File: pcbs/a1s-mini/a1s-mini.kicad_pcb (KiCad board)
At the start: 2 copper layers, 76 x 56 mm, 9 parts, among them IC1 3678, J5 Audio Out, U1 ESP32-DevKitC header, U2 CP2104 USB A board

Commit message: Starting A1S Mini, teardrops on sandwhich
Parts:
- removed IC1: 3678, DIY:Adafruit 3678
- removed JP1: SolderJumper_3_Bridged12, Jumper:SolderJumper-3_P1.3mm_Bridged12_RoundedPad1.0x1.5mm
- added 3V1: TestPoint_Small, TestPoint:TestPoint_Pad_D1.0mm, F.Cu at (108.4, 22.1)
- added 5V1: TestPoint_Small, TestPoint:TestPoint_Pad_D1.0mm, F.Cu at (109.5, 25.8)
- added C1: 0.1uF 50V, Capacitor_SMD:C_0805_2012Metric, F.Cu at (124.6, 60.8)
- added C10: 10uF, Capacitor_SMD:C_0805_2012Metric, F.Cu at (261.7, 126.9)
- added C11: 0.1uF 50V, Capacitor_SMD:C_0805_2012Metric, F.Cu at (261.7, 129.9)
- added C12: 10uF, Capacitor_SMD:C_0805_2012Metric, F.Cu at (257.5, 143.9)
- added C13: 10uF, Capacitor_SMD:C_0805_2012Metric, F.Cu at (127.3, 162.1)
- added C14: 0.1uF 50V, Capacitor_SMD:C_0805_2012Metric, F.Cu at (130.3, 162.1)
- added C15: 10uF, Capacitor_SMD:C_0805_2012Metric, F.Cu at (133.3, 162.1)
- added C2: 22uF, Capacitor_SMD:C_0805_2012Metric, F.Cu at (122.3, 60.8)
- added C3: 0.1uF 50V, Capacitor_SMD:C_0805_2012Metric, F.Cu at (152.0, 64.6)
- added C4: 0.1uF 50V, Capacitor_SMD:C_0805_2012Metric, F.Cu at (88.9, 121.0)
- added C5: 0.1uF 50V, Capacitor_SMD:C_0805_2012Metric, F.Cu at (65.8, 138.4)
- added C6: 22uF, Capacitor_SMD:C_0805_2012Metric, F.Cu at (138.7, 119.1)
- added C7: 22uF, Capacitor_SMD:C_0805_2012Metric, F.Cu at (135.6, 110.5)
- added C8: 0.1uF 50V, Capacitor_SMD:C_0805_2012Metric, F.Cu at (72.0, 97.9)
- added C9: 0.1uF 50V, Capacitor_SMD:C_0805_2012Metric, F.Cu at (78.1, 75.3)
- added D1: 2.1V G 10mA, LED_SMD:LED_0603_1608Metric, F.Cu at (135.2, 136.7)
- added D10: 1N5819HW-7-F, SamacSys_Parts:SOD3716X145N, F.Cu at (262.3, 147.1)
- added D11: LESD5D5.0CT1G, SamacSys_Parts:LESD5D50CT1G, F.Cu at (127.3, 166.2)
- added D12: LESD5D5.0CT1G, SamacSys_Parts:LESD5D50CT1G, F.Cu at (130.2, 166.2)
- added D13: LESD5D5.0CT1G, SamacSys_Parts:LESD5D50CT1G, F.Cu at (133.1, 166.2)
- added D14: 1N5819HW-7-F, SamacSys_Parts:SOD3716X145N, F.Cu at (137.9, 169.3)
- added D2: 2.1V G 10mA, LED_SMD:LED_0603_1608Metric, F.Cu at (135.2, 139.3)
- added D3: 2.1V G 10mA, LED_SMD:LED_0603_1608Metric, F.Cu at (250.4, 137.5)
- added D4: 2.1V G 10mA, LED_SMD:LED_0603_1608Metric, F.Cu at (250.4, 140.0)
- added D5: 2.1V O 10mA, LED_SMD:LED_0603_1608Metric, F.Cu at (131.8, 108.5)
- added D6: 2V R 10mA, LED_SMD:LED_0603_1608Metric, F.Cu at (154.6, 75.7)
- added D7: LESD5D5.0CT1G, SamacSys_Parts:LESD5D50CT1G, F.Cu at (254.2, 147.7)
- added D8: LESD5D5.0CT1G, SamacSys_Parts:LESD5D50CT1G, F.Cu at (252.1, 147.7)
- added D9: LESD5D5.0CT1G, SamacSys_Parts:LESD5D50CT1G, F.Cu at (258.5, 147.7)
- added DCD1: TestPoint_Small, TestPoint:TestPoint_Pad_D1.0mm, F.Cu at (110.2, 29.6)
- added GND1: TestPoint_Small, TestPoint:TestPoint_Pad_D1.0mm, F.Cu at (111.5, 33.8)
- added J1: UART1, Connector_PinHeader_2.54mm:PinHeader_1x04_P2.54mm_Vertical, F.Cu at (123.5, 162.2)
- added J2: SJ-3524-SMT-TR-PI, SamacSys_Parts:SJ3524SMTTRPI, F.Cu at (76.8, 135.0)
- added J3: Audio Out, Connector_PinHeader_2.54mm:PinHeader_1x03_P2.54mm_Vertical, F.Cu at (76.8, 110.8)
- added J4: UART0, Connector_PinHeader_2.54mm:PinHeader_1x04_P2.54mm_Vertical, F.Cu at (244.5, 119.8)
- added J6: USB4105-GF-A, DIY:GCT_USB4105-GF-A, F.Cu at (126.8, 156.5)
- added Q1: BC818, Package_TO_SOT_SMD:SOT-23, F.Cu at (68.8, 76.3)
- added Q2: BC818, Package_TO_SOT_SMD:SOT-23, F.Cu at (73.4, 76.0)
- added Q3: BC818, Package_TO_SOT_SMD:SOT-23, F.Cu at (228.2, 37.7)
- added Q4: BC818, Package_TO_SOT_SMD:SOT-23, F.Cu at (228.2, 42.2)
- added Q5: BC818, Package_TO_SOT_SMD:SOT-23, F.Cu at (228.2, 46.6)
- added R1: 1K 1%, Resistor_SMD:R_0805_2012Metric, F.Cu at (130.9, 136.9)
- added R10: 0R, Resistor_SMD:R_0805_2012Metric, F.Cu at (88.9, 126.9)
- added R11: 0R, Resistor_SMD:R_0805_2012Metric, F.Cu at (65.8, 144.3)
- added R12: 10K, Resistor_SMD:R_0805_2012Metric, F.Cu at (232.9, 37.0)
- added R13: 10K, Resistor_SMD:R_0805_2012Metric, F.Cu at (232.9, 39.9)
- added R14: 10K, Resistor_SMD:R_0805_2012Metric, F.Cu at (232.9, 42.9)
- added R15: 22.1K, Resistor_SMD:R_0805_2012Metric, F.Cu at (257.3, 119.6)
- added R16: 47.5K, Resistor_SMD:R_0805_2012Metric, F.Cu at (257.3, 122.6)
- added R17: 2K, Resistor_SMD:R_0805_2012Metric, F.Cu at (257.3, 125.5)
- added R18: 0R, Resistor_SMD:R_0805_2012Metric, F.Cu at (257.3, 128.5)
- added R19: 0R, Resistor_SMD:R_0805_2012Metric, F.Cu at (257.3, 131.4)
- added R2: 1K 1%, Resistor_SMD:R_0805_2012Metric, F.Cu at (130.9, 139.8)
- added R20: 5.1K 1%, Resistor_SMD:R_0805_2012Metric, F.Cu at (249.9, 147.7)
- added R21: 0R, Resistor_SMD:R_0805_2012Metric, F.Cu at (263.0, 152.7)
- added R22: 5.1K 1%, Resistor_SMD:R_0805_2012Metric, F.Cu at (256.4, 147.7)
- added R23: 22.1K, Resistor_SMD:R_0805_2012Metric, F.Cu at (122.6, 147.6)
- added R24: 47.5K, Resistor_SMD:R_0805_2012Metric, F.Cu at (125.6, 147.6)
- added R25: 2K, Resistor_SMD:R_0805_2012Metric, F.Cu at (128.5, 147.6)
- added R26: 0R, Resistor_SMD:R_0805_2012Metric, F.Cu at (131.5, 147.6)
- added R27: 0R, Resistor_SMD:R_0805_2012Metric, F.Cu at (134.4, 147.6)
- added R28: 5.1K 1%, Resistor_SMD:R_0805_2012Metric, F.Cu at (137.4, 147.6)
- added R29: 0R, Resistor_SMD:R_0805_2012Metric, F.Cu at (140.3, 147.6)
- added R3: 1K 1%, Resistor_SMD:R_0805_2012Metric, F.Cu at (246.1, 137.6)
- added R30: 5.1K 1%, Resistor_SMD:R_0805_2012Metric, F.Cu at (143.3, 147.6)
- added R4: 1K 1%, Resistor_SMD:R_0805_2012Metric, F.Cu at (246.1, 140.6)
- added R5: 1K 1%, Resistor_SMD:R_0805_2012Metric, F.Cu at (131.8, 110.5)
- added R6: 1K 1%, Resistor_SMD:R_0805_2012Metric, F.Cu at (154.7, 72.9)
- added R7: 0R, Resistor_SMD:R_0805_2012Metric, F.Cu at (148.0, 64.6)
- added R8: 22R 1%, Resistor_SMD:R_0805_2012Metric, F.Cu at (88.9, 124.0)
- added R9: 22R 1%, Resistor_SMD:R_0805_2012Metric, F.Cu at (65.8, 141.4)
- added S1: TL3305BF260QG, SamacSys_Parts:TL3305BF260QG, F.Cu at (74.2, 70.0)
- added S2: TL3305BF260QG, SamacSys_Parts:TL3305BF260QG, F.Cu at (77.5, 92.6)
- added U3: CP2102N, Package_DFN_QFN:QFN-28-1EP_5x5mm_P0.5mm_EP3.35x3.35mm, F.Cu at (263.1, 121.8)
- added U4: CP2102N, Package_DFN_QFN:QFN-28-1EP_5x5mm_P0.5mm_EP3.35x3.35mm, F.Cu at (138.5, 163.5)
- added VBUS1: TestPoint_Small, TestPoint:TestPoint_Pad_D1.0mm, F.Cu at (110.9, 37.2)
- J5: value Audio Out -> USB4105-GF-A; footprint Connector_PinHeader_2.54mm:PinHeader_1x03_P2.54mm_Vertical -> DIY:GCT_USB4105-GF-A
- U1: value ESP32-DevKitC header -> ESP32 A1S; footprint Espressif:ESP32-DevKitC -> Espressif:ESP32-WROVER-E_ThermalVias
- U2: value CP2104 USB A board -> AZ1117CH-3.3TRG1; footprint DIY:CP2104_USB_Board -> Package_TO_SOT_SMD:SOT-223-3_TabPin2; moved to F.Cu
- moved J5 150.2 mm to (254.1, 155.7), turned to 0 degrees
- moved H3 80.9 mm to (164.8, 35.0)
- moved H4 64.5 mm to (176.5, 36.9)
- moved H2 60.7 mm to (172.9, 29.0)
- moved U2 41.8 mm to (133.6, 116.3), turned to 90 degrees
- moved H1 39.0 mm to (155.6, 28.3)
- moved U1 32.0 mm to (135.9, 68.3)
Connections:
- U1 pad 1: +3.3V -> GND
- U1 pad 10: DIN -> unconnected-(U1-IO15-Pad10)
- U1 pad 11: BCLK -> IO2
- U1 pad 14: GND -> unconnected-(U1-MIC2N-Pad14)
- U1 pad 19: +5V -> GND
- U1 pad 2: unconnected-(U1-CHIP_PU-Pad2) -> +3.3V
- U1 pad 20: CLK -> GND
- U1 pad 21: D0 -> unconnected-(U1-LINEINR-Pad21)
- U1 pad 22: D1 -> unconnected-(U1-LINEINL-Pad22)
- U1 pad 23: GPIO15 -> unconnected-(U1-SPORP-Pad23)
- U1 pad 24: GPIO2 -> unconnected-(U1-SPORN-Pad24)
- U1 pad 25: GPIO0 -> unconnected-(U1-SPOLP-Pad25)
- U1 pad 26: GPIO4 -> unconnected-(U1-SPOLN-Pad26)
- U1 pad 27: GPIO16/U1RXD -> HPOUTL
- U1 pad 28: GPIO17/U1TXD -> HPOUTR
- U1 pad 29: GPIO5 -> unconnected-(U1-IO5-Pad29)
- U1 pad 30: GPIO18 -> IO18
- U1 pad 31: GPIO19 -> unconnected-(U1-IO23-Pad31)
- U1 pad 32: GND -> RXD1
- U1 pad 33: GPIO21 -> TXD1
- U1 pad 34: GPIO3/U0RXD -> unconnected-(U1-IO21-Pad34)
- U1 pad 35: GPIO1/U0TXD -> EN
- U1 pad 36: GPIO22 -> TXD0
- U1 pad 37: GPIO23 -> RXD0
- U1 pad 6: unconnected-(U1-VDET_2/GPIO35/ADC1_CH7-Pad6) -> IO0
- U1 pad 9: GPIO25 -> unconnected-(U1-IO13-Pad9)
- U2 pad 1: RST -> GND
- U2 pad 2: IO3 -> +3.3V
- U2 pad 3: IO2 -> +5V
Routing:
- net +5V: track 85.4 -> 0.00 mm
- net +3.3V: track 70.6 -> 0.00 mm
- net BCLK: track 37.3 -> 0.00 mm
- net DIN: track 34.3 -> 0.00 mm
- net GPIO25: track 33.1 -> 0.00 mm
- net GPIO16/U1RXD: track 22.4 -> 0.00 mm, vias 1 -> 0
- net GPIO17/U1TXD: track 22.1 -> 0.00 mm
- net GPIO4: track 13.7 -> 0.00 mm
- net ROUT: track 9.68 -> 0.00 mm
- net LOUT: track 9.68 -> 0.00 mm
- net AGND: track 9.68 -> 0.00 mm
- net DCD: track 6.35 -> 0.00 mm
- net GPIO5: track 2.54 -> 0.00 mm
- net GPIO3/U0RXD: track 2.54 -> 0.00 mm
- net GPIO23: track 2.54 -> 0.00 mm
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- removed copper zone on B.Cu, net GND
- removed copper zone on F.Cu, net GND
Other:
- board outline removed
- board text removed: "${TITLE} rev${REVISION} - (c) Martin Roger - ${ISSUE_DATE}"
- board text removed: "ANTENNA"
- board text removed: "G"
- board text removed: "GND"
- board text removed: "IO4"
- board text removed: "L"
- board text removed: "R"
- board text removed: "USB"

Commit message: Corrections and PCB layout
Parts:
- added JP1: SolderJumper_3_Bridged12, Jumper:SolderJumper-3_P1.3mm_Bridged12_RoundedPad1.0x1.5mm, F.Cu at (141.5, 101.3)
- added R31: 0R, Resistor_SMD:R_0603_1608Metric, F.Cu at (129.5, 113.8)
- C1, C11, C14, C3, C4, C5, C8, C9: footprint Capacitor_SMD:C_0805_2012Metric -> Capacitor_SMD:C_0603_1608Metric
- C10, C12, C13, C15: value 10uF -> 10uF 10V; footprint Capacitor_SMD:C_0805_2012Metric -> Capacitor_SMD:C_0603_1608Metric
- C2, C6, C7: value 22uF -> 22uF 10V
- D10, D14: footprint SamacSys_Parts:SOD3716X145N -> Diode_SMD:D_SOD-123
- D11, D12, D13, D7, D8, D9: value LESD5D5.0CT1G -> TVS 5.6V; footprint SamacSys_Parts:LESD5D50CT1G -> SamacSys_Parts:CPDUC5V0RHF
- R1, R10, R11, R18, R19, R2, R20, R21, R22, R26, R27, R28, R29, R3, R30, R4, R5, R6, R7, R8, R9: footprint Resistor_SMD:R_0805_2012Metric -> Resistor_SMD:R_0603_1608Metric
- R12, R13, R14: value 10K -> 10K 1%; footprint Resistor_SMD:R_0805_2012Metric -> Resistor_SMD:R_0603_1608Metric
- R15, R23: value 22.1K -> 22.1K 1%; footprint Resistor_SMD:R_0805_2012Metric -> Resistor_SMD:R_0603_1608Metric
- R16, R24: value 47.5K -> 47.5K 1%; footprint Resistor_SMD:R_0805_2012Metric -> Resistor_SMD:R_0603_1608Metric
- R17, R25: value 2K -> 2K 1%; footprint Resistor_SMD:R_0805_2012Metric -> Resistor_SMD:R_0603_1608Metric
- moved D4 145.4 mm to (123.4, 69.1), turned to -90 degrees
- moved D3 142.6 mm to (125.2, 69.1), turned to -90 degrees
- moved R3 137.4 mm to (127.0, 69.1), turned to -90 degrees
- moved R4 137.4 mm to (128.8, 69.1), turned to -90 degrees
- moved J4 135.3 mm to (120.7, 65.3), turned to 90 degrees
- moved R21 119.7 mm to (151.1, 110.0), turned to 180 degrees
- moved D10 118.1 mm to (151.6, 105.9), turned to -90 degrees
- moved C12 112.9 mm to (152.4, 102.6), turned to 180 degrees
- moved D9 112.9 mm to (153.7, 105.9)
- moved C11 111.3 mm to (155.7, 96.0)
- moved C10 111.0 mm to (155.7, 94.2)
- moved R16 107.7 mm to (153.2, 95.2), turned to 90 degrees
- moved U3 107.1 mm to (158.2, 100.1), turned to -90 degrees
- moved R17 107.1 mm to (153.4, 99.6)
- moved R15 106.2 mm to (153.4, 97.8)
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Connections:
- J5 pad A1_B12: Net-(J5-GND) -> GND
- J5 pad B1_A12: Net-(J5-GND) -> GND
- J6 pad A1_B12: Net-(J6-GND) -> GND
- J6 pad B1_A12: Net-(J6-GND) -> GND
- R21 pad 2: Net-(J5-GND) -> GND
- R29 pad 2: Net-(J6-GND) -> GND
- U1 pad 29: unconnected-(U1-IO5-Pad29) -> IO5
- U4 pad 1: GND -> /CP2102_1/DCD
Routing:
- net /CP2102_1/D+: track 0.00 -> 6.07 mm, vias 0 -> 2
- net /CP2102_1/D-: track 0.00 -> 5.78 mm
- net Net-(J6-CC1): track 0.00 -> 3.63 mm
- net Net-(J6-CC2): track 0.00 -> 2.98 mm
- added copper zone on B.Cu, net GND
- added copper zone on F.Cu, net GND
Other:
- board outline added: 69 x 56 mm

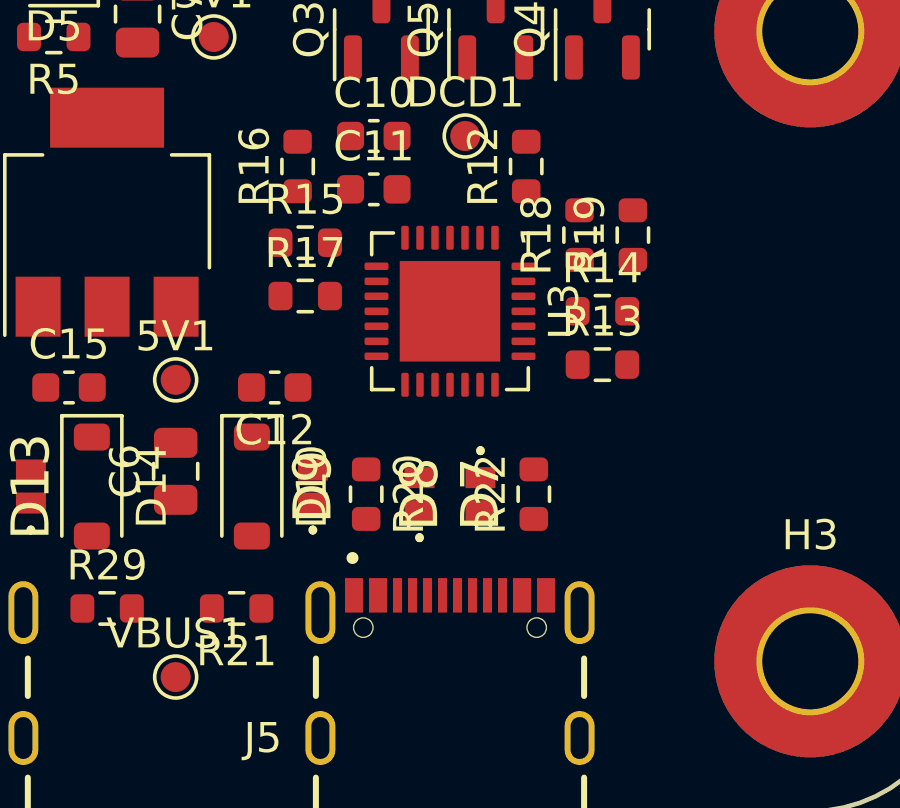
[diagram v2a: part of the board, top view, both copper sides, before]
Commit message: Progress on differential routing
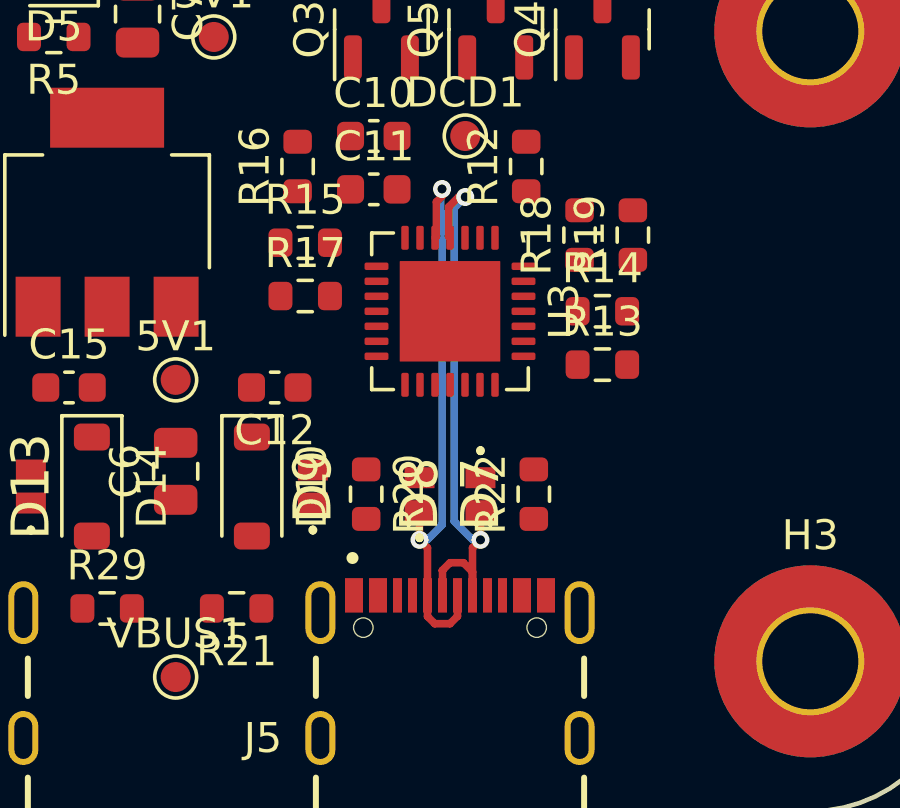
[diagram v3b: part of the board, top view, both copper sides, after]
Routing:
- net /CP2102_0/D+: track 0.00 -> 19.6 mm, vias 0 -> 2
- net /CP2102_0/D-: track 0.00 -> 19.5 mm, vias 0 -> 2
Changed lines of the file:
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@@
   (gr_arc locked (start 159.752 85.744) (mid 158.69134 85.30466) (end 158.252 84.244)
     (stroke (width 0.15) (type default)) (layer "Edge.Cuts"))
+  (segment (start 157.992 109.545) (end 157.992 108.716) (width 0.254) (layer "F.Cu") (net 19))
+  (segment (start 157.992 108.716) (end 157.988 108.712) (width 0.254) (layer "F.Cu") (net 19))
+  (segment (start 158.992 109.545) (end 158.992 107.962) (width 0.254) (layer "F.Cu") (net 19))
+  (segment (start 158.242 108.458) (end 158.6888 108.458) (width 0.254) (layer "F.Cu") (net 19))
+  (segment (start 158.992 108.7612) (end 158.992 109.545) (width 0.254) (layer "F.Cu") (net 19))
+  (segment (start 158.195201 96.600168) (end 158.195201 97.579201) (width 0.254) (layer "F.Cu") (net 19))
+  (segment (start 158.195201 97.579201) (end 158.242 97.626) (width 0.254) (layer "F.Cu") (net 19))
+  (segment (start 157.988 108.712) (end 158.242 108.458) (width 0.254) (layer "F.Cu") (net 19))
+  (segment (start 158.6888 108.458) (end 158.992 108.7612) (width 0.254) (layer "F.Cu") (net 19))
+  (segment (start 159.258 107.696) (end 159.258 106.722) (width 0.254) (layer "F.Cu") (net 19))
+  (segment (start 158.529369 96.266) (end 158.195201 96.600168) (width 0.254) (layer "F.Cu") (net 19))
+  (segment (start 158.992 107.962) (end 159.258 107.696) (width 0.254) (layer "F.Cu") (net 19))
+  (segment (start 158.75 96.266) (end 158.529369 96.266) (width 0.254) (layer "F.Cu") (net 19))
+  (via (at 159.258 107.696) (size 0.6) (drill 0.3) (layers "F.Cu" "B.Cu") (net 19))
+  (via (at 158.75 96.266) (size 0.6) (drill 0.3) (layers "F.Cu" "B.Cu") (net 19))
+  (segment (start 158.75 96.266) (end 158.382386 96.633614) (width 0.254) (layer "B.Cu") (net 19))
+  (segment (start 158.382386 107.074386) (end 159.004 107.696) (width 0.254) (layer "B.Cu") (net 19))
+  (segment (start 159.004 107.696) (end 159.258 107.696) (width 0.254) (layer "B.Cu") (net 19))
+  (segment (start 158.382386 96.633614) (end 158.382386 107.074386) (width 0.254) (layer "B.Cu") (net 19))
   (segment (start 138.684 106.722) (end 138.684 107.472001) (width 0.254) (layer "F.Cu") (net 21))
   (segment (start 140.45 109.545) (end 140.45 108.556691) (width 0.254) (layer "F.Cu") (net 21))
@@
   (segment (start 139.57825 108.366252) (end 139.176999 107.965001) (width 0.254) (layer "B.Cu") (net 21))
   (segment (start 140.640439 108.366252) (end 139.57825 108.366252) (width 0.254) (layer "B.Cu") (net 21))
+  (segment (start 157.975986 96.244645) (end 157.975986 95.999986) (width 0.254) (layer "F.Cu") (net 22))
+  (segment (start 158.492 109.545) (end 158.492 110.24) (width 0.254) (layer "F.Cu") (net 22))
+  (segment (start 157.742 97.626) (end 157.788799 97.579201) (width 0.254) (layer "F.Cu") (net 22))
+  (segment (start 157.788799 97.579201) (end 157.788799 96.431832) (width 0.254) (layer "F.Cu") (net 22))
+  (segment (start 157.734 110.49) (end 157.492 110.248) (width 0.254) (layer "F.Cu") (net 22))
+  (segment (start 157.492 109.545) (end 157.492 107.962) (width 0.254) (layer "F.Cu") (net 22))
+  (segment (start 157.788799 96.431832) (end 157.975986 96.244645) (width 0.254) (layer "F.Cu") (net 22))
+  (segment (start 157.492 107.962) (end 157.226 107.696) (width 0.254) (layer "F.Cu") (net 22))
+  (segment (start 157.226 107.696) (end 157.226 106.722) (width 0.254) (layer "F.Cu") (net 22))
+  (segment (start 158.492 110.24) (end 158.242 110.49) (width 0.254) (layer "F.Cu") (net 22))
+  (segment (start 158.242 110.49) (end 157.734 110.49) (width 0.254) (layer "F.Cu") (net 22))
+  (segment (start 157.492 110.248) (end 157.492 109.545) (width 0.254) (layer "F.Cu") (net 22))
+  (via (at 157.975986 95.999986) (size 0.6) (drill 0.3) (layers "F.Cu" "B.Cu") (net 22))
+  (via (at 157.226 107.696) (size 0.6) (drill 0.3) (layers "F.Cu" "B.Cu") (net 22))
+  (segment (start 157.928614 96.047358) (end 157.975986 95.999986) (width 0.254) (layer "B.Cu") (net 22))
+  (segment (start 157.48 107.696) (end 157.975986 107.200014) (width 0.254) (layer "B.Cu") (net 22))
+  (segment (start 157.928614 96.77201) (end 157.928614 96.047358) (width 0.254) (layer "B.Cu") (net 22))
+  (segment (start 157.975986 96.819382) (end 157.928614 96.77201) (width 0.254) (layer "B.Cu") (net 22))
+  (segment (start 157.975986 107.200014) (end 157.975986 96.819382) (width 0.254) (layer "B.Cu") (net 22))
+  (segment (start 157.226 107.696) (end 157.48 107.696) (width 0.254) (layer "B.Cu") (net 22))
   (segment (start 140.716 107.472001) (end 139.9032 108.284801) (width 0.254) (layer "F.Cu") (net 23))
   (segment (start 140.716 106.722) (end 140.716 107.472001) (width 0.254) (layer "F.Cu") (net 23))

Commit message: Advancing routing
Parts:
- moved D11 2.05 mm to (140.7, 105.9)
- moved D12 2.05 mm to (138.7, 105.9)
- moved R7 1.20 mm to (153.5, 88.5)
- moved C3 1.20 mm to (151.8, 88.5)
- moved Q3 0.80 mm to (156.2, 89.9)
- moved Q4 0.76 mm to (163.3, 89.9), turned to -90 degrees
- moved Q5 0.76 mm to (159.8, 89.9)
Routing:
- net VBUS: track 0.00 -> 53.7 mm, vias 0 -> 3
- net IO0: track 0.00 -> 38.7 mm, vias 0 -> 2
- net IO2: track 0.00 -> 37.8 mm, vias 0 -> 2
- net RTS0: track 0.00 -> 24.3 mm, vias 0 -> 2
- net TXD0: track 0.00 -> 23.7 mm, vias 0 -> 2
- net RXD0: track 0.00 -> 23.2 mm, vias 0 -> 2
- net Net-(Q5-B): track 0.00 -> 16.6 mm
- net Net-(Q4-B): track 0.00 -> 14.8 mm
- net DTR0: track 0.00 -> 14.5 mm, vias 0 -> 2
- net /CP2102_1/D-: track 5.78 -> 19.0 mm, vias 0 -> 2
- net /CP2102_1/D+: track 6.07 -> 19.0 mm
- net Net-(Q3-B): track 0.00 -> 8.76 mm
- net EN: track 0.00 -> 6.77 mm
- net Net-(U3-RXD): track 0.00 -> 4.36 mm
- net Net-(U3-VBUS): track 0.00 -> 4.04 mm
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- added copper zone on F.Cu, net +5V
- added copper zone on F.Cu, net VBUS
